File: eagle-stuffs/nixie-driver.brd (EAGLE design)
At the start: 94.9 x 69.8 mm, 65 parts, among them IC1 74141N/K155ID1, IC2 74LS595N, IC4 NE555, Q1 MPSA92, Q10 2N2222, Q11 IRF840, Q12 2N2222, Q2 MPSA92, Q3 MPSA92, Q4 MPSA92, Q5 MPSA42, Q6 MPSA42, Q7 MPSA42, Q8 MPSA42, Q9 PN2907, U1 MC34063DIP

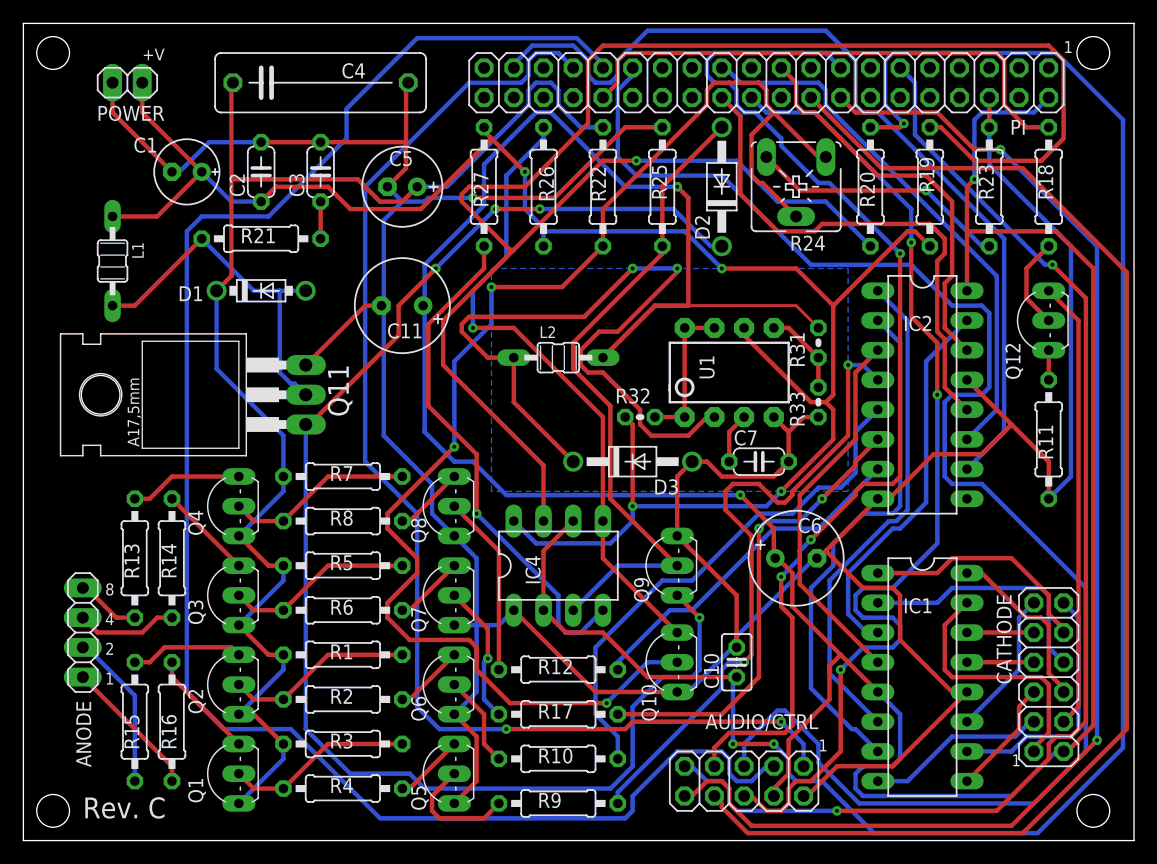
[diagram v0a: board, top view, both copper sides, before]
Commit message: Change fixed resistors for voltage output ajust. to pot.
The PI seems to be quite touchy about the voltage drop under load. Got
to push it to 5.1v to make the red led stop to blink!
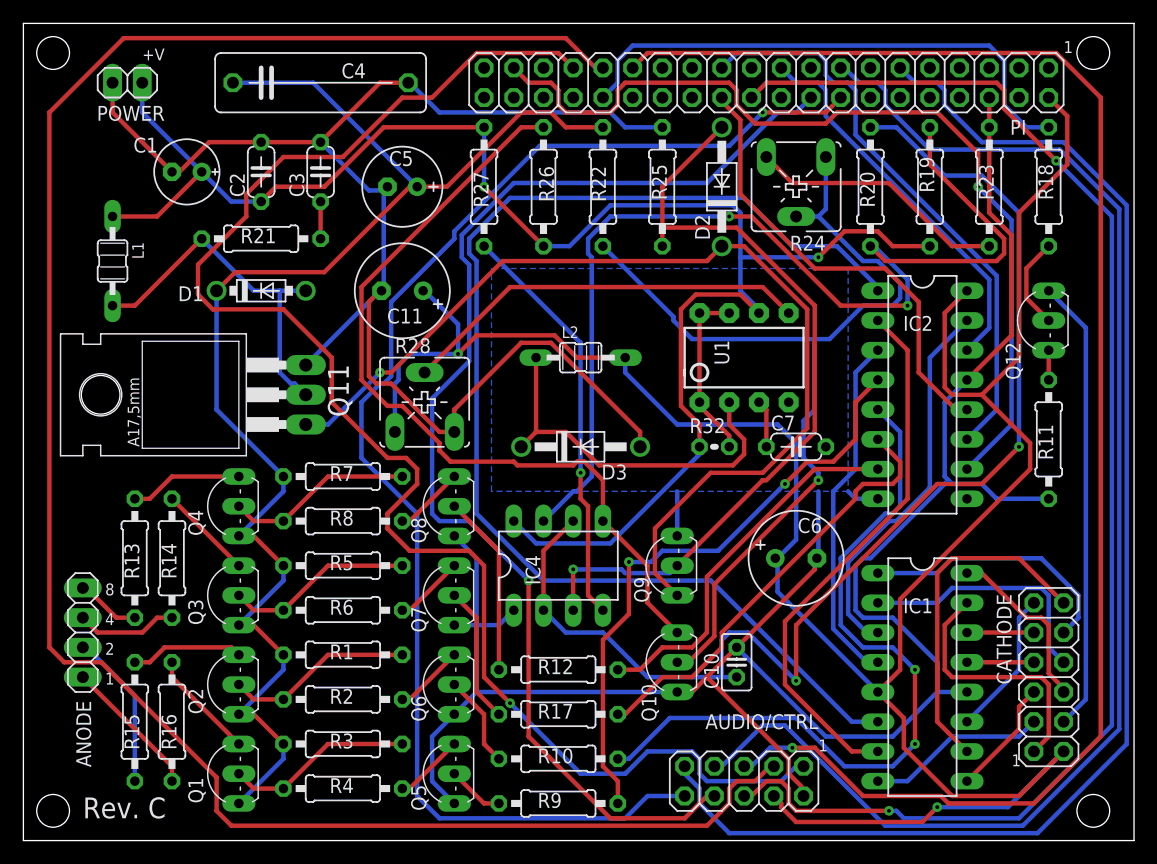
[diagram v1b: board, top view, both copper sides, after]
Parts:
- removed R31: 3.6k, resistor:0204V
- removed R33: 1.1k, resistor:0204V
- added R28: 10k, pot:CA6V
- L2: value 100uH/1A -> 47uH/1.5A
- moved R32 6.84 mm to (59.1, 33.7)
- moved D3 4.62 mm to (47.6, 33.7)
- moved C7 3.42 mm to (66.0, 33.7)
- moved L2 1.91 mm to (47.6, 41.3)
- moved U1 1.80 mm to (61.6, 41.3)
- moved C11 1.27 mm to (32.4, 47.0)
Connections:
- removed net N$67: R31.1, R33.2, U1.5
- new net N$61: R28.S, U1.5
- net +5V: now also R28.A; no longer R31.2
- net GND: now also R28.E; no longer R33.1
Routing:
- net N$52: track 153.1 -> 89.6 mm, vias 1 -> 2
- net N$13: track 42.7 -> 105.3 mm
- net N$66: track 159.3 -> 104.9 mm, vias 3 -> 2
- net +5V: track 251.6 -> 202.9 mm, vias 3 -> 2
- net N$62: track 122.1 -> 84.6 mm, vias 4 -> 1
- net N$64: track 117.6 -> 82.3 mm, vias 3 -> 1
- net N$61: track 0.00 -> 35.1 mm
- net N$69: track 65.3 -> 32.5 mm, vias 2 -> 0
- net N$55: track 87.5 -> 117.8 mm, vias 3 -> 2
- net N$48: track 144.6 -> 169.5 mm
- net N$50: track 92.9 -> 117.0 mm, vias 3 -> 0
- net N$47: track 106.8 -> 130.0 mm, vias 2 -> 1
- net N$39: track 44.9 -> 65.3 mm, vias 0 -> 2
- net +12V: track 162.0 -> 145.1 mm, vias 4 -> 2
- net N$60: track 55.0 -> 69.6 mm, vias 1 -> 0
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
